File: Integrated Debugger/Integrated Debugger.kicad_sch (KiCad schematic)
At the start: 15 parts, among them J1 B2B GT-B0353FSV06-08B0201, J2 USB_C (PC <-> Host), U1 USBULC6-2M6

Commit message: feat: swap debugger rgb led part
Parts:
- D1: footprint Picoballoon ICs:WS2812B-2020 -> Picoballoon ICs:WS2812B-2121; symbol Picoballoon ICs:WS2812B-2020 -> Picoballoon ICs:WS2812B-2121
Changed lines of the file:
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@@
 	)
 	(symbol
-		(lib_id "Picoballoon ICs:WS2812B-2020")
+		(lib_id "Picoballoon ICs:WS2812B-2121")
 		(at 64.77 46.99 0)
 		(mirror y)
@@
 			)
 		)
-		(property "Footprint" "Picoballoon ICs:WS2812B-2020"
+		(property "Footprint" "Picoballoon ICs:WS2812B-2121"
 			(at 63.5 54.61 0)
 			(effects
@@
 			)
 		)
-		(property "Description" "RGB LED with integrated controller, 2.0 x 2.0 mm, 12 mA"
+		(property "Description" "RGB LED with integrated controller, 2.1 x 2.1 mm, 12 mA"
 			(at 34.29 59.69 0)
 			(effects

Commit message: feat: change debugger part mnf data
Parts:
- D1: JLCPCB Part # C965555 -> C5349957; LCSC Part # C965555 -> C5349957; MPN WS2812B-2020 -> XL-2121RGBC-WS2812B
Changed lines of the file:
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@@
 			)
 		)
-		(property "LCSC Part #" "C965555"
+		(property "LCSC Part #" "C5349957"
 			(at 64.77 46.99 0)
 			(effects
@@
 			)
 		)
-		(property "MPN" "WS2812B-2020"
+		(property "MPN" "XL-2121RGBC-WS2812B"
 			(at 64.77 46.99 0)
 			(effects
@@
 			)
 		)
-		(property "JLCPCB Part #" "C965555"
+		(property "JLCPCB Part #" "C5349957"
 			(at 64.77 46.99 0)
 			(effects

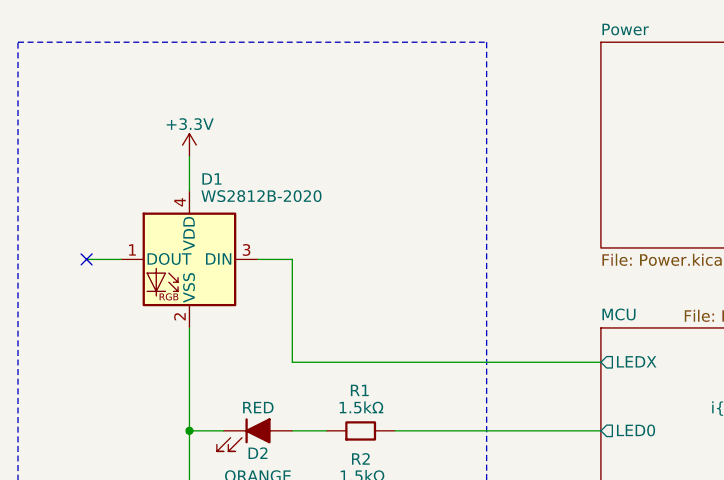
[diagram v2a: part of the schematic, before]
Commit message: Change diode
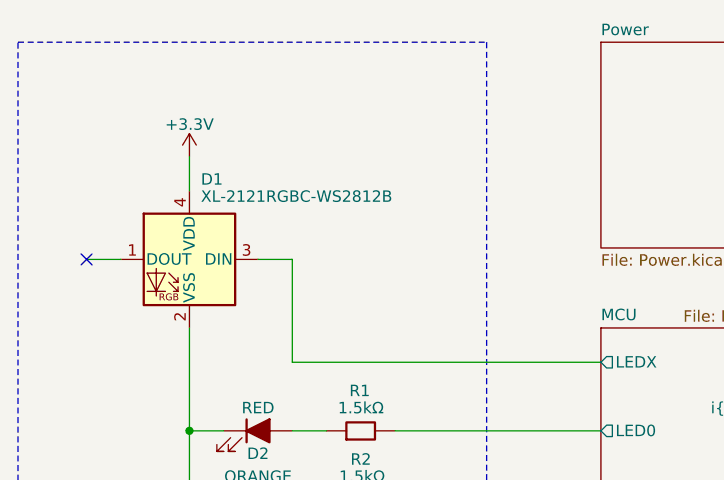
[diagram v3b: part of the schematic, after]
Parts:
- D1: value WS2812B-2020 -> XL-2121RGBC-WS2812B; JLCPCB Part # C5349957 -> (none)
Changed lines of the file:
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@@
 			)
 		)
-		(property "Value" "WS2812B-2020"
+		(property "Value" "XL-2121RGBC-WS2812B"
 			(at 66.04 40.005 0)
 			(effects
@@
 			(at 64.77 46.99 0)
 			(effects
-				(font
-					(size 1.27 1.27)
-				)
-				(hide yes)
-			)
-		)
-		(property "JLCPCB Part #" "C5349957"
-			(at 64.77 46.99 0)
-			(effects

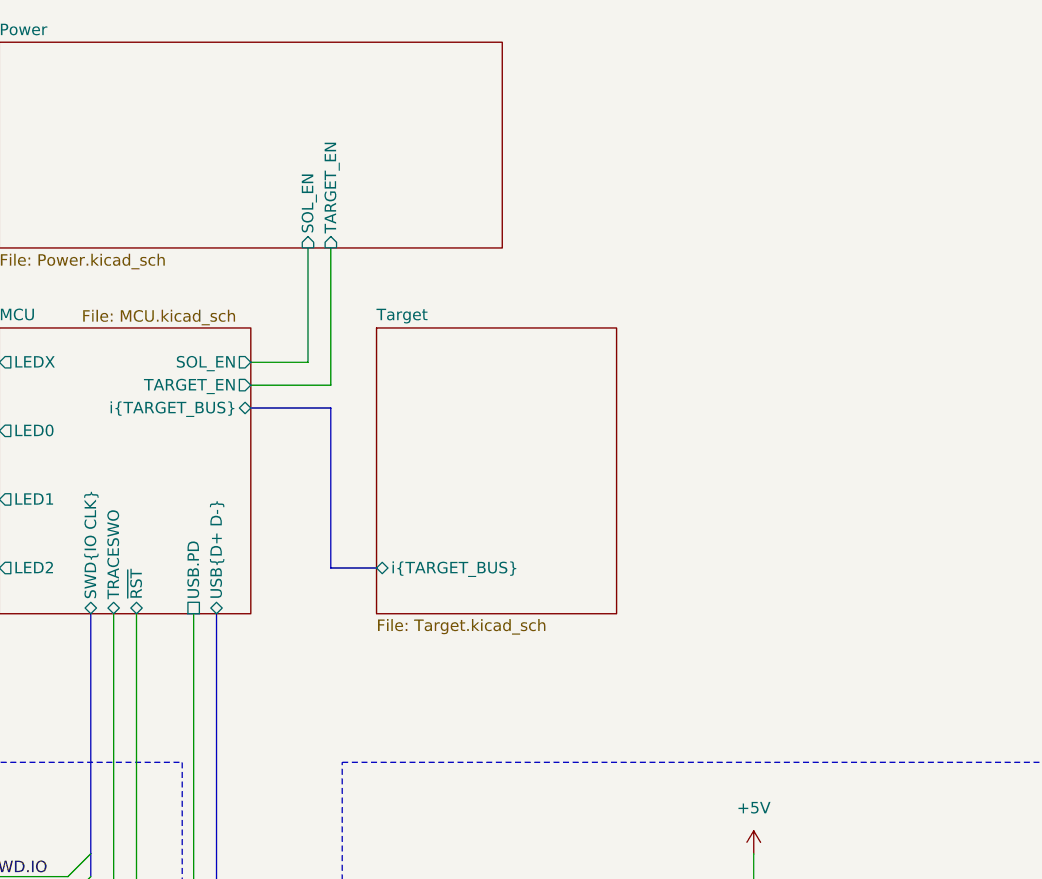
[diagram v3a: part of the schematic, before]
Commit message: feat: fix debugger bugs & impl. auxiliary power - 869b0p9f3
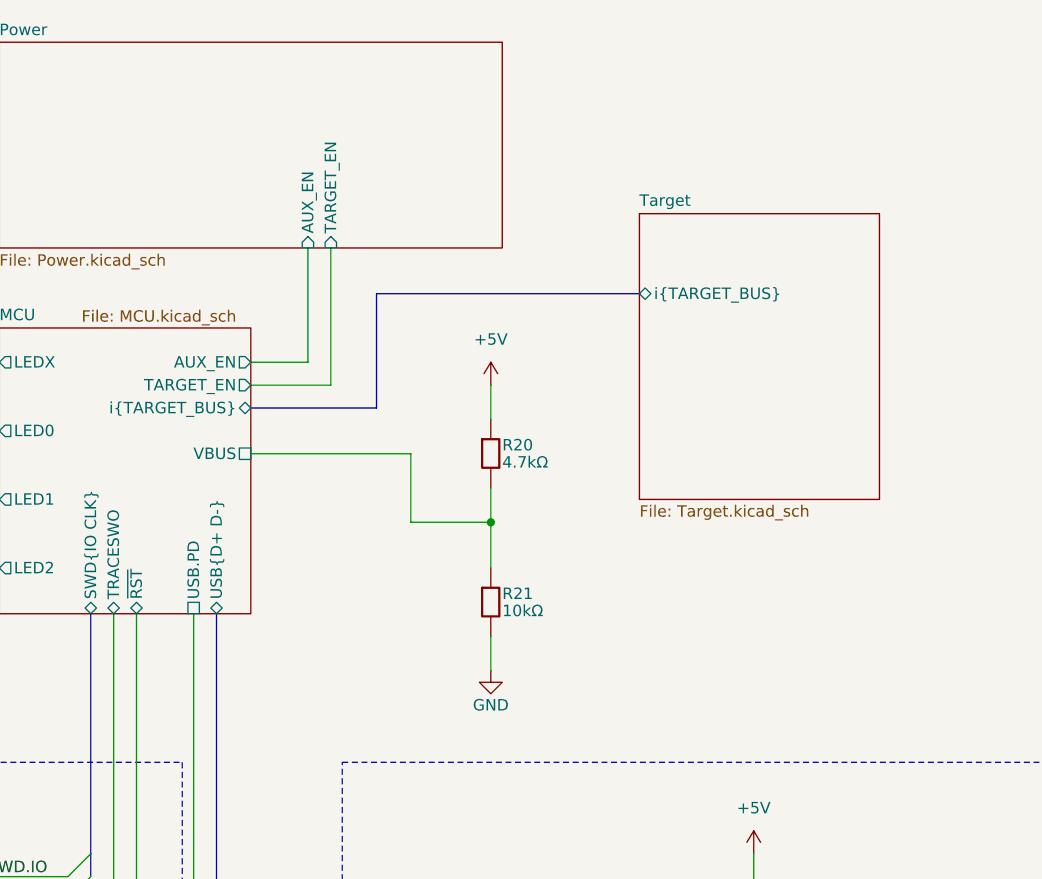
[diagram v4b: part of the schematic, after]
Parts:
- added R20: 4.7kΩ, Picoballoon Passives:Resistor 0201, symbol Picoballoon Passives:Resistor
- added R21: 10kΩ, Picoballoon Passives:Resistor 0201, symbol Picoballoon Passives:Resistor
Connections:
- net +5V: now also R20.1
- net GND: now also R21.2
- new net MCU/VBUS: R20.2, R21.1
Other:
- sheet MCU ports: added AUX_EN, VBUS; removed SOL_EN
- sheet Power ports: added AUX_EN; removed SOL_EN

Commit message: IDBG schematic
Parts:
- removed D1: XL-2121RGBC-WS2812B, Picoballoon ICs:WS2812B-2121, symbol Picoballoon ICs:WS2812B-2121
- removed J2: USB_C (PC <-> Host), Picoballoon Mechanical & Misc:USB-C DX07S016JA1R1500, symbol Picoballoon Mechanical & Misc:USB-C DX07S016JA1R1500
- removed R7, R8: 1.5kΩ, Picoballoon Passives:Resistor 0201, symbol Picoballoon Passives:Resistor
- removed U1: USBULC6-2M6, Picoballoon ICs:UQFN-6, symbol Picoballoon ICs:USBULC6-2M6
- added C8: 4.7nF, Picoballoon Passives:Capacitor 0603, symbol Picoballoon Passives:Capacitor
- added C9: 10μF, Picoballoon Passives:Capacitor 0402, symbol Picoballoon Passives:Capacitor
- added FB1, FB3: 1000Ω, Picoballoon Passives:Inductor 0402, symbol Picoballoon Passives:Ferrite bead
- added J6: TYPE-C-31-M-12, Picoballoon Mechanical & Misc:TYPE-C-31-M-12, symbol Picoballoon Mechanical & Misc:TYPE-C-31-M-12
- added R14: 1MΩ, Picoballoon Passives:Resistor 0603, symbol Picoballoon Passives:Resistor
- added R15, R22: 5.1kΩ, Picoballoon Passives:Resistor 0201, symbol Picoballoon Passives:Resistor
- added U5: USBLC6-2P6, Picoballoon ICs:SOT-666-6, symbol Picoballoon ICs:USBULC6-2M6
- D2: JLCPCB Part # C3646923 -> (none)
- D3: value ORANGE -> GREEN; JLCPCB Part # C5440629 -> (none); LCSC Part # C5440629 -> C5366341; MPN XL-0201UOC -> APG0603ZGC-5MAV
- D4: value YELLOW -> BLUE; JLCPCB Part # C5440628 -> (none); LCSC Part # C5440628 -> C3646921; MPN XL-0201UYC -> XL-0201UBC
- R1: value 1.5kΩ -> 560Ω; JLCPCB Part # C155737 -> (none); LCSC Part # C155737 -> C295808; MPN RC0201FR-071K5L -> RC0201FR-07560RL
- R2, R3: value 1.5kΩ -> 470Ω; JLCPCB Part # C155737 -> (none); LCSC Part # C155737 -> C852285; MPN RC0201FR-071K5L -> RT0201DRD07470RL
- R20: JLCPCB Part # C138135 -> (none)
- R21: JLCPCB Part # C717002 -> (none)
- R4: JLCPCB Part # C155737 -> (none)
- R5, R6: JLCPCB Part # C155743 -> (none)
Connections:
- net D+: now also J6.A6 (D+), J6.B6 (D+), U5.3 (I/O2)
- net D-: now also J6.A7 (D-), J6.B7 (D-), U5.1 (I/O1)
- net GND: now also C8.2, C9.2, J6.A1 (GND), J6.A12 (GND), J6.B1 (GND), J6.B12 (GND), R14.2, R15.2, R22.2, U5.2 (GND)
- net USBX.D+: now also U5.4 (I/O2)
- net USBX.D-: now also U5.6 (I/O1)
- net +3.3V renamed Pin_9
- net Pin_9: now also FB3.1
- net +5V renamed VDD_USB
- net VDD_USB: now also C9.1, FB1.1, U5.5 (VBUS)
- net MCU/TRACESWO: no longer names the net of J1.6 (Pin_6)
- new net: FB1.2, J6.A4 (VBUS), J6.A9 (VBUS), J6.B4 (VBUS), J6.B9 (VBUS)
- new net: J6.A5 (CC1), R22.1
- new net: J6.B5 (CC2), R15.1
- new net SHLD: C8.1, J6.S1 (SHIELD), J6.S2 (SHIELD), J6.S3 (SHIELD), J6.S4 (SHIELD), R14.1
- new net VDD_3V3: FB3.2
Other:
- sheet MCU ports: added none; removed LEDX, TRACESWO
- note added: "HOST SWD"
- note added: "USB 2.0 TYPE-C"
- note removed: "SERIAL WIRE DEBUG"
- note removed: "USER INTERFACE"
- moved on the sheet: D2, D3, D4, J1, R1, R2, R20, R21, R3, R4, R5, R6

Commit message: Integrated debugger PCB
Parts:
- removed FB3: 1000Ω, Picoballoon Passives:Inductor 0402, symbol Picoballoon Passives:Ferrite bead
- D2: value RED -> ERR; footprint Picoballoon Passives:LED 0201 -> Picoballoon Passives:LED 0402
- D3: value GREEN -> ACT; footprint Picoballoon Passives:LED 0201 -> Picoballoon Passives:LED 0402
- D4: value BLUE -> SER; footprint Picoballoon Passives:LED 0201 -> Picoballoon Passives:LED 0402
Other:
- sheet MCU ports: added TG_EN; removed TARGET_EN
- sheet Power ports: added TG_EN; removed TARGET_EN
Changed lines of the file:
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@@
 	)
 	(rectangle
-		(start 66.04 105.41)
+		(start 76.2 105.41)
 		(end 129.54 140.97)
 		(stroke
@@
 			)
 		)
-		(property "Value" "BLUE"
+		(property "Value" "SER"
 			(at 72.39 85.09 0)
 			(do_not_autoplace yes)
@@
 			)
 		)
-		(property "Footprint" "Picoballoon Passives:LED 0201"
+		(property "Footprint" "Picoballoon Passives:LED 0402"
 			(at 72.39 82.55 0)
 			(effects
@@
 	(symbol
 		(lib_id "Picoballoon Power Symbols:+3.3V")
-		(at 82.55 125.73 90)
+		(at 90.17 125.73 90)
 		(unit 1)
 		(exclude_from_sim no)
@@
 		(dnp no)
 		(property "Reference" "#PWR03"
-			(at 86.36 125.73 0)
+			(at 93.98 125.73 0)
 			(effects
 				(font
@@
 		)
 		(property "Value" "VDD_3V3"
-			(at 79.375 125.73 90)
+			(at 86.995 125.73 90)
 			(do_not_autoplace yes)
 			(effects
@@
 		)
 		(property "Footprint" ""
-			(at 82.55 125.73 0)
+			(at 90.17 125.73 0)
 			(effects
 				(font
@@
 		)
 		(property "Datasheet" ""
-			(at 82.55 125.73 0)
+			(at 90.17 125.73 0)
 			(effects
 				(font
@@
 		)
 		(property "Description" "Power symbol creates a global label with name \"+3.3V\""
-			(at 82.55 125.73 0)
+			(at 90.17 125.73 0)
 			(effects
 				(font
@@
 			)
 		)
-		(property "Value" "RED"
+		(property "Value" "ERR"
 			(at 72.39 69.85 0)
 			(do_not_autoplace yes)
@@
 			)
 		)
-		(property "Footprint" "Picoballoon Passives:LED 0201"
+		(property "Footprint" "Picoballoon Passives:LED 0402"
 			(at 72.39 67.31 0)
 			(effects
@@
 			)
 		)
-		(property "Value" "GREEN"
+		(property "Value" "ACT"
 			(at 72.39 77.47 0)
 			(do_not_autoplace yes)
@@
 			)
 		)
-		(property "Footprint" "Picoballoon Passives:LED 0201"
+		(property "Footprint" "Picoballoon Passives:LED 0402"
 			(at 72.39 74.93 0)
 			(effects
@@
 	)
 	(symbol
-		(lib_id "Picoballoon Passives:Ferrite bead")
-		(at 86.36 125.73 270)
-		(unit 1)
-		(exclude_from_sim no)
-		(in_bom yes)
-		(on_board yes)
-		(dnp no)
-		(property "Reference" "FB3"
-			(at 86.36 128.905 90)
-			(do_not_autoplace yes)
-			(effects
-				(font
-					(size 1.27 1.27)
-				)
-			)
-		)
-		(property "Value" "1000Ω"
-			(at 86.36 130.81 90)
-			(do_not_autoplace yes)
-			(effects
-				(font
-					(size 1.27 1.27)
-				)
-			)
-		)
-		(property "Footprint" "Picoballoon Passives:Inductor 0402"
-			(at 86.36 123.952 90)
-			(effects
-				(font
-					(size 1.27 1.27)
-				)
-				(hide yes)
-			)
-		)
-		(property "Datasheet" "~"
-			(at 86.36 125.73 0)
-			(effects
-				(font
-					(size 1.27 1.27)
-				)
-				(hide yes)
-			)
-		)
-		(property "Description" "Generic Ferrite bead"
-			(at 86.36 125.73 0)
-			(effects
-				(font
-					(size 1.27 1.27)
-				)
-				(hide yes)
-			)
-		)
-		(property "MPN" "BLM15HD102SN1D"
-			(at 86.36 125.73 0)
-			(effects
-				(font
-					(size 1.27 1.27)
-				)
-				(hide yes)
-			)
-		)
-		(property "LCSC Part #" "C21516"
-			(at 86.36 125.73 90)
-			(effects
-				(font
-					(size 1.27 1.27)
-				)
-				(hide yes)
-			)
-		)
-		(pin "1"
-		)
-		(pin "2"
-		)
-		(instances
-			(project "Integrated Debugger"
-				(path "/ce538ebe-fda9-4af3-9f8c-9fd5bf58f0e4"
-					(reference "FB3")
-					(unit 1)
-				)
-			)
-		)
-	)
-	(symbol
 		(lib_id "Picoballoon Power Symbols:VBUS")
 		(at 193.04 99.06 0)
@@
 			)
 		)
-		(pin "TARGET_EN" input
+		(pin "TG_EN" input
 			(at 147.32 46.99 270)
 			(effects
@@
 			)
 		)
-		(pin "TARGET_EN" output
+		(pin "TG_EN" output
 			(at 138.43 62.23 0)
 			(effects
